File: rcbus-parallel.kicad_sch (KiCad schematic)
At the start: 15 parts, among them J2 Conn_02x20_Odd_Even, P1 Conn_01x39, SW1 SW_DIP_x06, U1 82C55A_PLCC, U2 74HCT688, U3 74HCT04

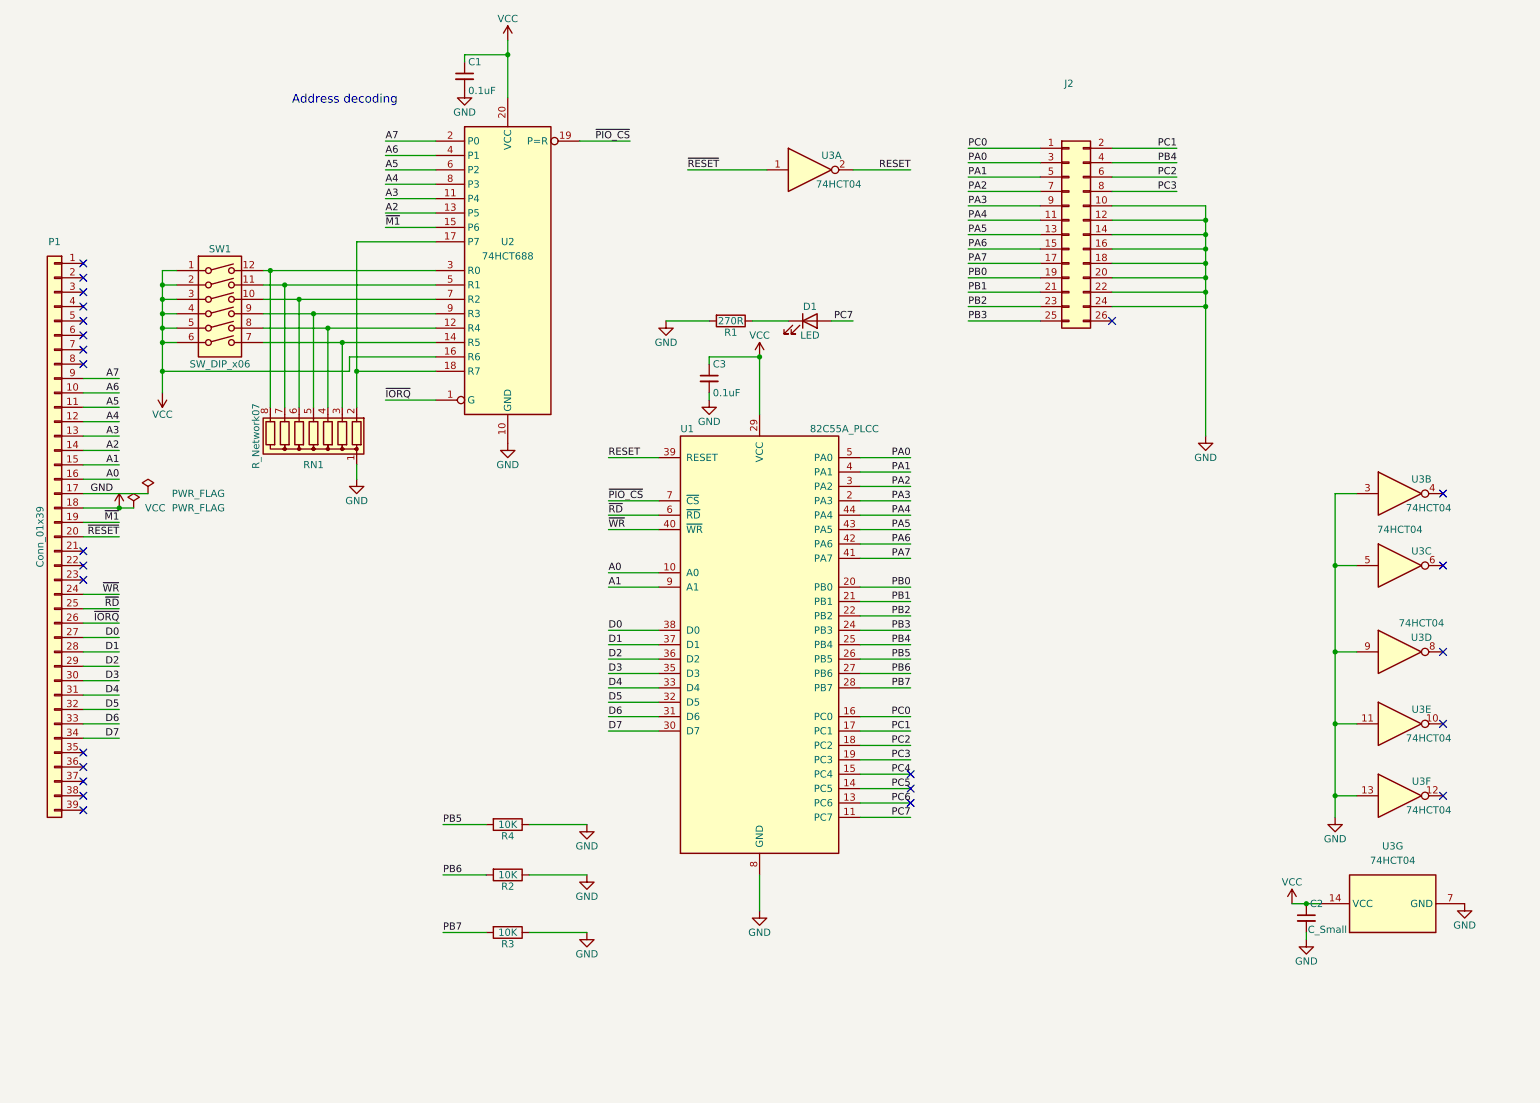
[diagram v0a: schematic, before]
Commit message: add git submodule library and kibot build stuff
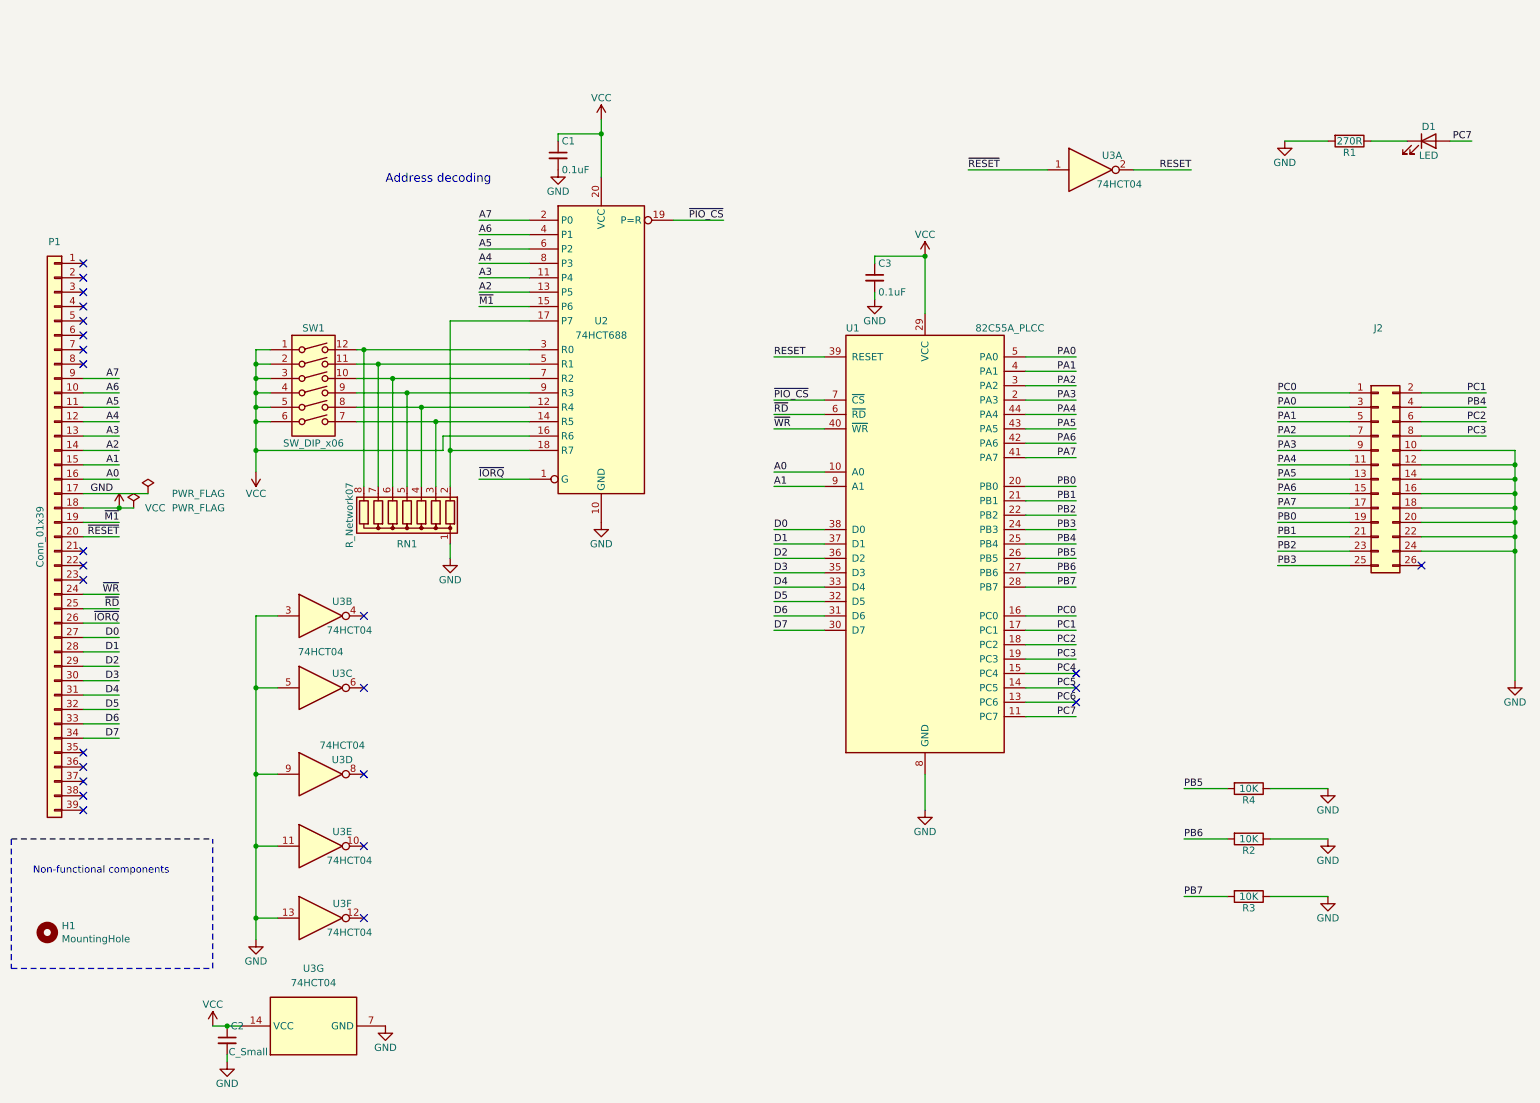
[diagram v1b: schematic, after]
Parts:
- added H1: MountingHole, MountingHole:MountingHole_3.2mm_M3, symbol Mechanical:MountingHole
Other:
- note added: "Non-functional components"
- moved on the sheet: C1, C2, C3, D1, J2, R1, R2, R3, R4, RN1, SW1, U1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

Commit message: reorg and routing
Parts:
- removed D1: LED, LED_THT:LED_D3.0mm, symbol Device:LED
- removed R1: 270R, Resistor_THT:R_Axial_DIN0207_L6.3mm_D2.5mm_P7.62mm_Horizontal, symbol Device:R
- removed SW1: SW_DIP_x06, Button_Switch_THT:SW_DIP_SPSTx06_Slide_9.78x17.42mm_W7.62mm_P2.54mm, symbol Switch:SW_DIP_x06
- added J1: Conn_02x06_Odd_Even, Connector_PinHeader_2.54mm:PinHeader_2x06_P2.54mm_Vertical, symbol Connector_Generic:Conn_02x06_Odd_Even
- J2: footprint Connector_PinHeader_2.54mm:PinHeader_2x13_P2.54mm_Horizontal -> Connector_IDC:IDC-Header_2x13_P2.54mm_Horizontal
- U1: footprint Package_LCC:PLCC-44 -> Package_LCC:PLCC-44_THT-Socket
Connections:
- net VCC: now also J1.1 (Pin_1), J1.11 (Pin_11), J1.3 (Pin_3), J1.5 (Pin_5), J1.7 (Pin_7), J1.9 (Pin_9)
- net at RN1.4 (R3), U2.12 (R4): now also J1.10 (Pin_10)
- net at RN1.3 (R2), U2.14 (R5): now also J1.12 (Pin_12)
- net at RN1.8 (R7), U2.3 (R0): now also J1.2 (Pin_2)
- net at RN1.7 (R6), U2.5 (R1): now also J1.4 (Pin_4)
- net at RN1.6 (R5), U2.7 (R2): now also J1.6 (Pin_6)
- net at RN1.5 (R4), U2.9 (R3): now also J1.8 (Pin_8)
- no-connect marks 25 -> 26
